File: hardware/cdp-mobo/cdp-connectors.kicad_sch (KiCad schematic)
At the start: 11 parts, among them J1 Conn_02x20_Odd_Even, J2 Conn_01x09_Pin, J3 Conn_01x07_Pin, J4 Conn_01x05_Pin, J5 Conn_01x02_Pin, J6 Conn_01x04_Pin

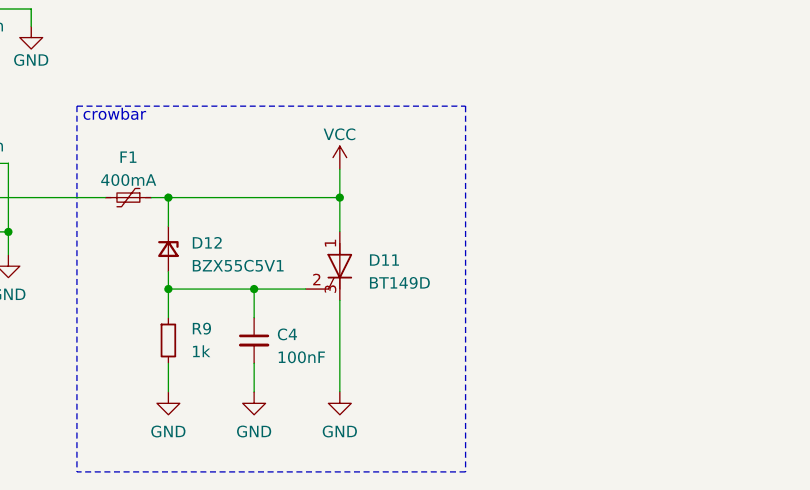
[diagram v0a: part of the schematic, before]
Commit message: Minor changes in component values, and added a the IO module.
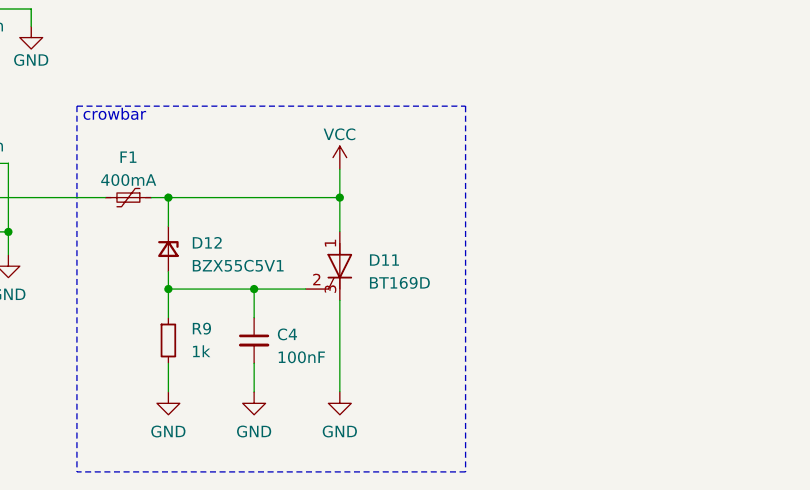
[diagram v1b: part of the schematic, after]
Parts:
- D11: value BT149D -> BT169D
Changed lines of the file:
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@@
       (effects (font (size 1.27 1.27)) (justify left))
     )
-    (property "Value" "BT149D" (at 94.615 161.29 0)
+    (property "Value" "BT169D" (at 94.615 161.29 0)
       (effects (font (size 1.27 1.27)) (justify left))
     )
